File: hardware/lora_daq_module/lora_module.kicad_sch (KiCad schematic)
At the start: 0 parts

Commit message: update schematic properties
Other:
- company: (none) -> ECE Capstone Team 14 at Portland State University
- title: (none) -> lora module subcircuit
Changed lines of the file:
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@@
 	(generator_version "9.0")
 	(paper "A4")
+	(title_block
+		(title "lora module subcircuit")
+		(date "2025-10-16")
+		(rev "rev0")
+		(company "ECE Capstone Team 14 at Portland State University")
+		(comment 1 "drawn by daniel monahan")
+	)
 )

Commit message: add chips and start wiring USBC Recept. & UART bridge
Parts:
- added J1: USB_C_Receptacle, symbol Connector:USB_C_Receptacle
- added R1, R2: 5.1k, symbol Device:R_Small_US
- added U1: LoRa-E5, symbol LoRa-E5:LoRa-E5
- added U2: CAT24C256, symbol Memory_EEPROM:CAT24C256
- added U3: CP2102N-Axx-xQFN20, Package_DFN_QFN:SiliconLabs_QFN-20-1EP_3x3mm_P0.5mm, symbol Interface_USB:CP2102N-Axx-xQFN20
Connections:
- new net: J1.A1 (GND), J1.A12 (GND), J1.B1 (GND), J1.B12 (GND)
- new net: J1.A4 (VBUS), J1.A9 (VBUS), J1.B4 (VBUS), J1.B9 (VBUS)
- new net: J1.A5 (CC1), R2.1
- new net: J1.A6 (D+), J1.B6 (D+)
- new net: J1.A7 (D-), J1.B7 (D-)
- new net: J1.B5 (CC2), R1.1
- new net: U3.12 (GND), U3.21 (GND), U3.3 (GND)
- new net GND: R1.2, R2.2
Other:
- note added: "5.1k pulldowns disable PD & establish board as sink"
- note added: "USB Input and UART Bridge"

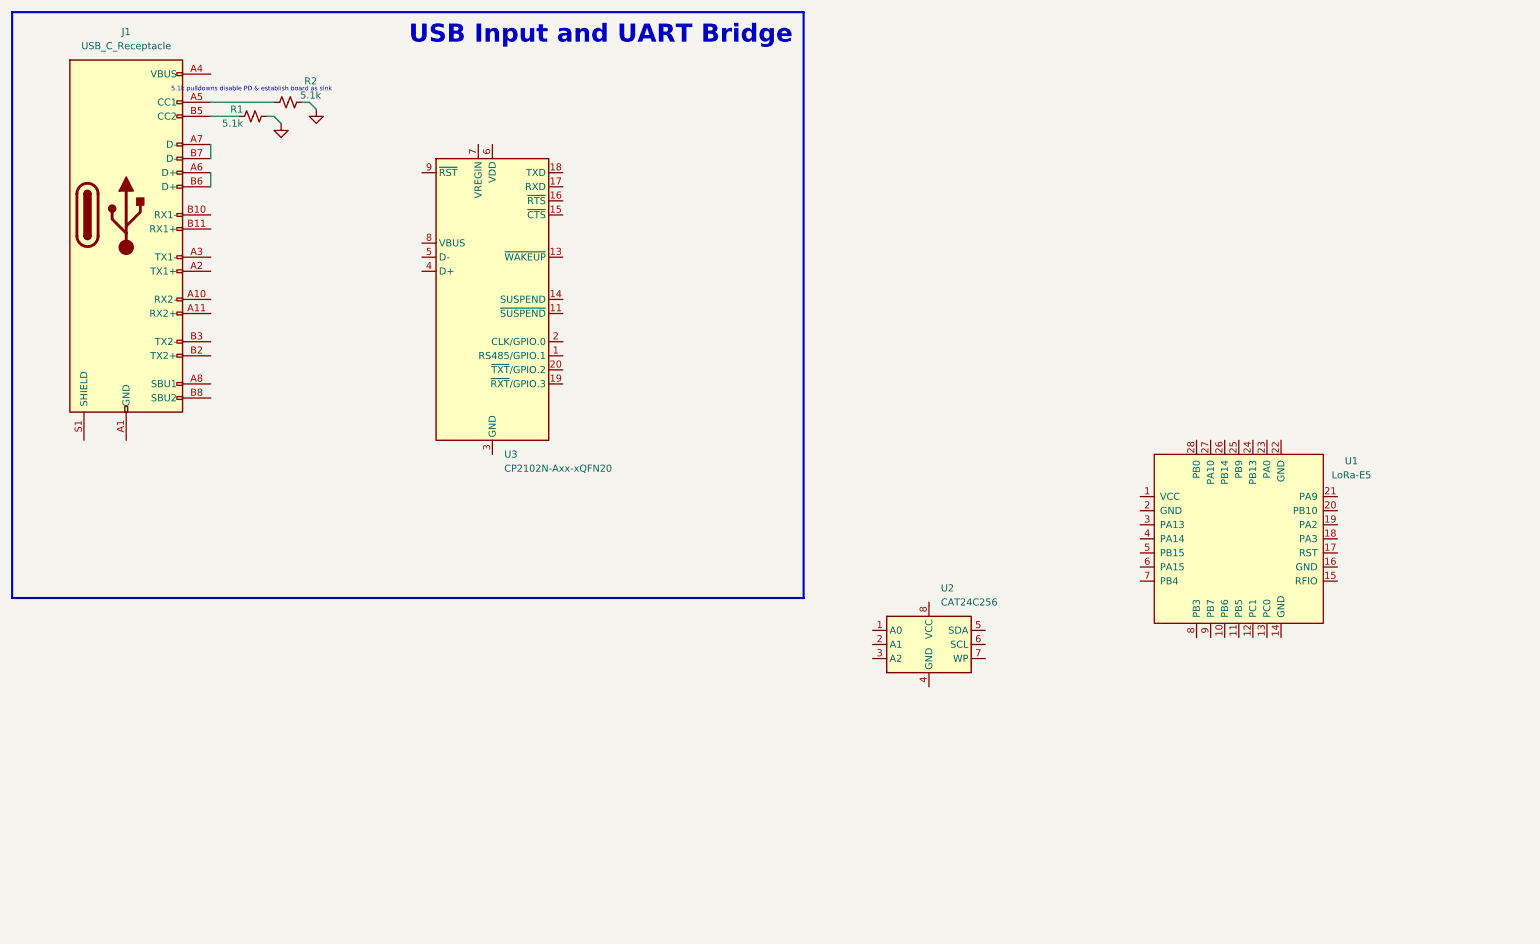
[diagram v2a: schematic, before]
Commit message: added eeprom support, antenna connector, and general connections needed for rev0 schematic
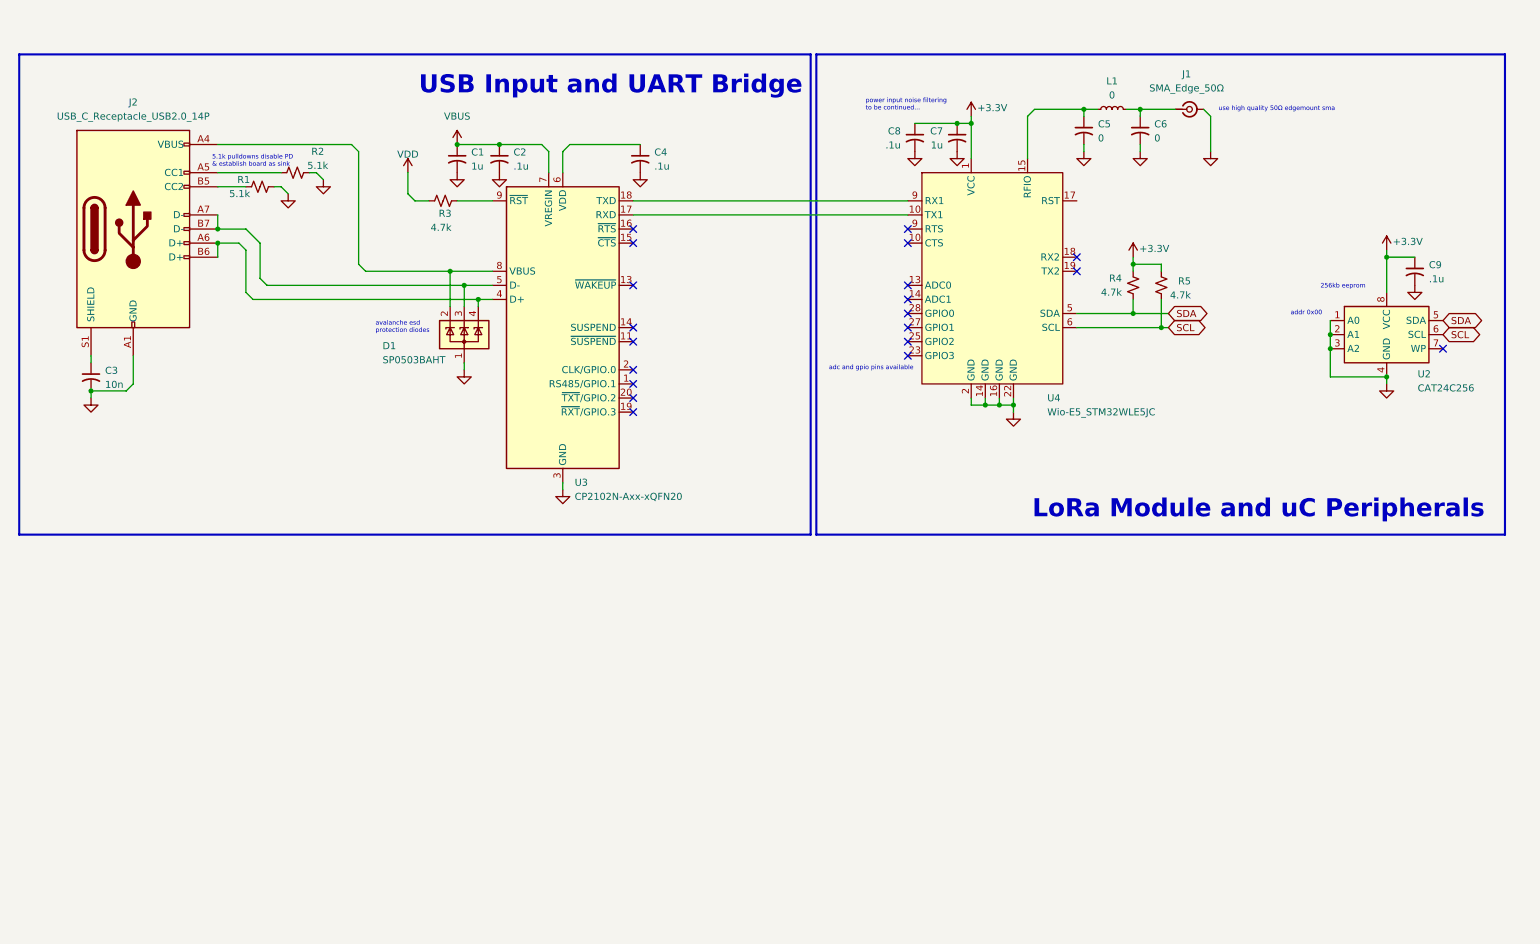
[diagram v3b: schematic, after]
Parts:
- removed J1: USB_C_Receptacle, symbol Connector:USB_C_Receptacle
- removed U1: LoRa-E5, symbol LoRa-E5:LoRa-E5
- added C1, C7: 1u, symbol Device:C_Small_US
- added C2, C4, C8, C9: .1u, symbol Device:C_Small_US
- added C3: 10n, symbol Device:C_Small_US
- added C5, C6: 0, symbol Device:C_Small_US
- added D1: SP0503BAHT, Package_TO_SOT_SMD:SOT-143, symbol Power_Protection:SP0503BAHT
- added J1: SMA_Edge_50Ω, symbol Connector:Conn_Coaxial_Small
- added J2: USB_C_Receptacle_USB2.0_14P, symbol Connector:USB_C_Receptacle_USB2.0_14P
- added L1: 0, symbol Device:L_Small
- added R3, R4, R5: 4.7k, symbol Device:R_Small_US
- added U4: Wio-E5_STM32WLE5JC, symbol wio_e5:Wio_E5
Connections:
- net GND: now also U2.1 (A0), U2.2 (A1), U2.3 (A2), U2.4 (GND), U3.12 (GND), U3.21 (GND), U3.3 (GND), C1.2, C2.2, C3.2, C4.2, C5.2, C6.2, C7.2, C8.2, C9.2, D1.1 (A), J1.2 (Ext), J2.A1 (GND), J2.A12 (GND), J2.B1 (GND), J2.B12 (GND), U4.14 (GND), U4.16 (GND), U4.2 (GND), U4.22 (GND)
- net at R2.1: now also J2.A5 (CC1)
- net at R1.1: now also J2.B5 (CC2)
- net SDA: now reaches U2.5 (SDA)
- net SDA: now also R4.1, U4.5 (SDA)
- net SCL: now reaches U2.6 (SCL)
- net SCL: now also R5.1, U4.6 (SCL)
- net +3.3V: now reaches U2.8 (VCC)
- net +3.3V: now also C7.1, C8.1, C9.1, R4.2, R5.2, U4.1 (VCC)
- net at U3.17 (RXD): now also U4.10 (CTS)
- net at U3.18 (TXD): now also U4.9 (RTS)
- net at U3.4 (D+): now also D1.4 (K), J2.A6 (D+), J2.B6 (D+)
- net at U3.5 (D-): now also D1.3 (K), J2.A7 (D-), J2.B7 (D-)
- net at U3.6 (VDD): now also C4.1
- net VBUS: now reaches U3.7 (VREGIN)
- net VBUS: now also C1.1, C2.1
- net at U3.8 (VBUS): now also D1.2 (K), J2.A4 (VBUS), J2.A9 (VBUS), J2.B4 (VBUS), J2.B9 (VBUS)
- net at U3.9 (~{RST}): now also R3.2
- new net: C3.1, J2.S1 (SHIELD)
- new net: C6.1, J1.1 (In), L1.2
- new net: C5.1, L1.1, U4.15 (RFIO)
- new net VDD: R3.1
- no-connect marks 0 -> 20
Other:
- note added: "256kb eeprom"
- note added: "LoRa Module and uC Peripherals"
- note added: "adc and gpio pins available"
- note added: "addr 0x00"
- note added: "avalanche esd protection diodes"
- note added: "power input noise filtering to be continued..."
- note added: "use high quality 50Ω edgemount sma"
- moved on the sheet: R1, R2, U2, U3

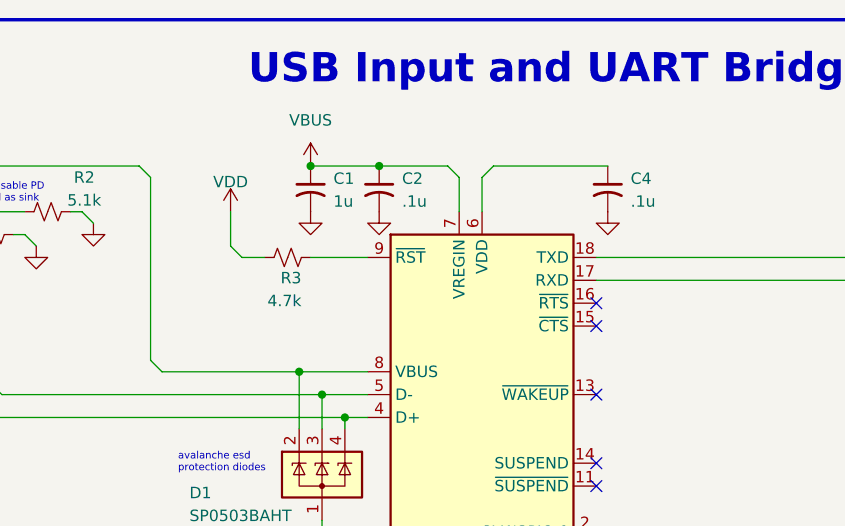
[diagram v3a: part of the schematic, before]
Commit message: schematic documentation
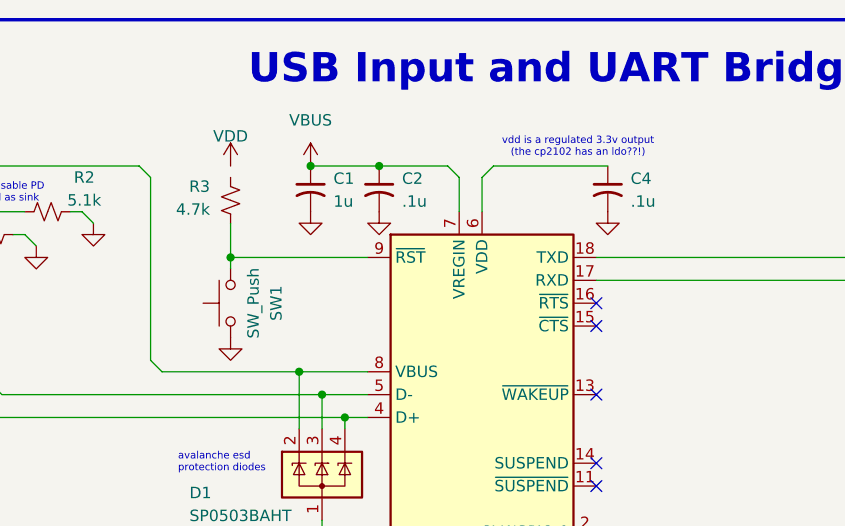
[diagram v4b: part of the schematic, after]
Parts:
- added SW1: SW_Push, symbol Switch:SW_Push
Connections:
- net GND: now also SW1.1
- net VDD: no longer R3.1
- net at U4.10 (CTS): now also U3.17 (RXD)
- net at U4.9 (RTS): now also U3.18 (TXD)
- net at U3.9 (~{RST}): now also R3.1, SW1.2; no longer R3.2
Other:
- note added: "vdd is a regulated 3.3v output (the cp2102 has an ldo??!)"
- moved on the sheet: R3
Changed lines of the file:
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@@
 		)
 	)
+	(text "vdd is a regulated 3.3v output\n(the cp2102 has an ldo??!)"
+		(exclude_from_sim no)
+		(at 123.698 34.798 0)
+		(effects
+			(font
+				(size 0.8128 0.8128)
+			)
+		)
+	)
 	(text "avalanche esd \nprotection diodes"
 		(exclude_from_sim no)
@@
 	)
 	(junction
+		(at 85.09 46.99)
+		(diameter 0)
+		(color 0 0 0 0)
+	)
+	(junction
 		(at 220.98 69.85)
 		(diameter 0)
@@
 	(wire
 		(pts
-			(xy 86.36 46.99) (xy 88.9 46.99)
+			(xy 95.25 62.23) (xy 100.33 62.23)
 		)
 		(stroke
@@
 	(wire
 		(pts
-			(xy 95.25 62.23) (xy 100.33 62.23)
+			(xy 217.17 36.83) (xy 217.17 38.1)
 		)
 		(stroke
@@
 	(wire
 		(pts
-			(xy 217.17 36.83) (xy 217.17 38.1)
+			(xy 101.6 36.83) (xy 109.22 36.83)
 		)
 		(stroke
@@
 	(wire
 		(pts
-			(xy 101.6 36.83) (xy 109.22 36.83)
+			(xy 194.31 82.55) (xy 194.31 83.82)
 		)
 		(stroke
@@
 	(wire
 		(pts
-			(xy 194.31 82.55) (xy 194.31 83.82)
+			(xy 67.31 41.91) (xy 68.58 41.91)
 		)
 		(stroke
@@
 	(wire
 		(pts
-			(xy 67.31 41.91) (xy 68.58 41.91)
+			(xy 85.09 43.18) (xy 85.09 46.99)
 		)
 		(stroke
@@
 	(wire
 		(pts
-			(xy 86.36 46.99) (xy 85.09 45.72)
-		)
-		(stroke
-			(width 0)
-			(type default)
-		)
-	)
-	(wire
-		(pts
 			(xy 113.03 97.79) (xy 113.03 99.06)
 		)
@@
 	(wire
 		(pts
-			(xy 93.98 46.99) (xy 100.33 46.99)
+			(xy 186.69 82.55) (xy 186.69 83.82)
 		)
 		(stroke
@@
 	(wire
 		(pts
-			(xy 186.69 82.55) (xy 186.69 83.82)
+			(xy 125.73 46.99) (xy 175.26 46.99)
 		)
 		(stroke
@@
 	(wire
 		(pts
-			(xy 125.73 46.99) (xy 175.26 46.99)
+			(xy 55.88 55.88) (xy 55.88 63.5)
 		)
 		(stroke
@@
 	(wire
 		(pts
-			(xy 55.88 55.88) (xy 55.88 63.5)
+			(xy 85.09 48.26) (xy 85.09 46.99)
 		)
 		(stroke
@@
 	(wire
 		(pts
-			(xy 85.09 41.91) (xy 85.09 45.72)
+			(xy 58.42 60.96) (xy 59.69 62.23)
 		)
 		(stroke
@@
 	(wire
 		(pts
-			(xy 58.42 60.96) (xy 59.69 62.23)
+			(xy 113.03 41.91) (xy 113.03 38.1)
 		)
 		(stroke
@@
 	(wire
 		(pts
-			(xy 113.03 41.91) (xy 113.03 38.1)
+			(xy 50.8 49.53) (xy 50.8 52.07)
 		)
 		(stroke
@@
 	(wire
 		(pts
-			(xy 50.8 49.53) (xy 50.8 52.07)
+			(xy 50.8 36.83) (xy 74.93 36.83)
 		)
 		(stroke
@@
 	(wire
 		(pts
-			(xy 50.8 36.83) (xy 74.93 36.83)
+			(xy 251.46 71.12) (xy 251.46 73.66)
 		)
 		(stroke
@@
 	(wire
 		(pts
-			(xy 251.46 71.12) (xy 251.46 73.66)
+			(xy 251.46 78.74) (xy 261.62 78.74)
 		)
 		(stroke
@@
 	(wire
 		(pts
-			(xy 251.46 78.74) (xy 261.62 78.74)
+			(xy 85.09 46.99) (xy 100.33 46.99)
 		)
 		(stroke
@@
 	(symbol
 		(lib_id "Device:R_Small_US")
-		(at 91.44 46.99 90)
+		(at 85.09 40.64 180)
 		(unit 1)
 		(exclude_from_sim no)
@@
 		(dnp no)
 		(property "Reference" "R3"
-			(at 92.964 49.276 90)
+			(at 82.804 39.116 0)
 			(effects
 				(font
@@
 		)
 		(property "Value" "4.7k"
-			(at 92.964 51.816 90)
+			(at 82.804 41.656 0)
 			(effects
 				(font
@@
 		)
 		(property "Footprint" ""
-			(at 91.44 46.99 0)
+			(at 85.09 40.64 0)
 			(effects
 				(font
@@
 		)
 		(property "Datasheet" "~"
-			(at 91.44 46.99 0)
+			(at 85.09 40.64 0)
 			(effects
 				(font
@@
 		)
 		(property "Description" "Resistor, small US symbol"
-			(at 91.44 46.99 0)
+			(at 85.09 40.64 0)
 			(effects
 				(font
@@
 	)
 	(symbol
+		(lib_id "Switch:SW_Push")
+		(at 85.09 52.07 90)
+		(unit 1)
+		(exclude_from_sim no)
+		(in_bom yes)
+		(on_board yes)
+		(dnp no)
+		(property "Reference" "SW1"
+			(at 90.17 52.07 0)
+			(effects
+				(font
+					(size 1.27 1.27)
+				)
+			)
+		)
+		(property "Value" "SW_Push"
+			(at 87.63 52.07 0)
+			(effects
+				(font
+					(size 1.27 1.27)
+				)
+			)
+		)
+		(property "Footprint" ""
+			(at 80.01 52.07 0)
+			(effects
+				(font
+					(size 1.27 1.27)
+				)
+				(hide yes)
+			)
+		)
+		(property "Datasheet" "~"
+			(at 80.01 52.07 0)
+			(effects
+				(font
+					(size 1.27 1.27)
+				)
+				(hide yes)
+			)
+		)
+		(property "Description" "Push button switch, generic, two pins"
+			(at 77.47 51.308 0)
+			(effects
+				(font
+					(size 1.27 1.27)
+				)
+				(hide yes)
+			)
+		)
+		(pin "1"
+		)
+		(pin "2"
+		)
+		(instances
+			(project ""
+				(path "/3a75d17e-6505-4097-95c7-feffd430343e/b2d61906-71c1-4ea1-893f-6962d616acd4"
+					(reference "SW1")
+					(unit 1)
+				)
+			)
+		)
+	)
+	(symbol
 		(lib_id "Connector:Conn_Coaxial_Small")
 		(at 226.06 30.48 0)
@@
 	(symbol
 		(lib_id "power:VDD")
-		(at 85.09 41.91 0)
+		(at 85.09 36.83 0)
 		(unit 1)
 		(exclude_from_sim no)
@@
 		(dnp no)
 		(property "Reference" "#PWR012"
-			(at 85.09 45.72 0)
+			(at 85.09 40.64 0)
 			(effects
 				(font
@@
 		)
 		(property "Value" "VDD"
-			(at 85.09 38.608 0)
+			(at 85.09 33.528 0)
 			(effects
 				(font
@@
 		)
 		(property "Footprint" ""
-			(at 85.09 41.91 0)
+			(at 85.09 36.83 0)
 			(effects
 				(font
@@
 		)
 		(property "Datasheet" ""
-			(at 85.09 41.91 0)
+			(at 85.09 36.83 0)
 			(effects
 				(font
@@
 		)
 		(property "Description" "Power symbol creates a global label with name \"VDD\""
-			(at 85.09 41.91 0)
+			(at 85.09 36.83 0)
 			(effects
 				(font
@@
 					(unit 1)
 				)
+			)
+		)
+	)
+	(symbol
+		(lib_id "power:GND")
+		(at 85.09 55.88 0)
+		(unit 1)
+		(exclude_from_sim no)
+		(in_bom yes)
+		(on_board yes)
+		(dnp no)
+		(fields_autoplaced yes)
+		(property "Reference" "#PWR014"
+			(at 85.09 62.23 0)
+			(effects
+				(font
+					(size 1.27 1.27)
+				)
+				(hide yes)
+			)
+		)
+		(property "Value" "GND"
+			(at 85.09 60.96 0)
+			(effects
+				(font
+					(size 1.27 1.27)
+				)
+				(hide yes)
+			)
+		)
+		(property "Footprint" ""
+			(at 85.09 55.88 0)
+			(effects
+				(font
+					(size 1.27 1.27)
+				)
+				(hide yes)
+			)
+		)
+		(property "Datasheet" ""
+			(at 85.09 55.88 0)
+			(effects
+				(font
+					(size 1.27 1.27)
+				)
+				(hide yes)
+			)
+		)
+		(property "Description" "Power symbol creates a global label with name \"GND\" , ground"
+			(at 85.09 55.88 0)
+			(effects
+				(font
+					(size 1.27 1.27)
+				)
+				(hide yes)
+			)
+		)
+		(pin "1"
+		)
+		(instances
+			(project "lora_daq_module"
+				(path "/3a75d17e-6505-4097-95c7-feffd430343e/b2d61906-71c1-4ea1-893f-6962d616acd4"
+					(reference "#PWR014")
+					(unit 1)
+				)

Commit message: post design review comments
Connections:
- net VDD: now also R3.2
- net at U4.10 (CTS): now also U3.17 (RXD)
- net at U4.9 (RTS): now also U3.18 (TXD)
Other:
- note added: "*add connector and spi input for SD card"
- note added: "*add subghz, make sure xtal pins match wio-e5, add swi interface"
- note added: "*common-mode choke"
- note added: "*gpio for 3.3en, 5en"
- note added: "*jumper here"
- note added: "*match table 1 on datasheet"
